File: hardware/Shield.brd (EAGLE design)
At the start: 55.9 x 47 mm, 26 parts, among them J1 AVR_SPI_PRG_6PTH, J2 TMR, J3 RELAY, Q8 TIP120, Y1 16Mhz

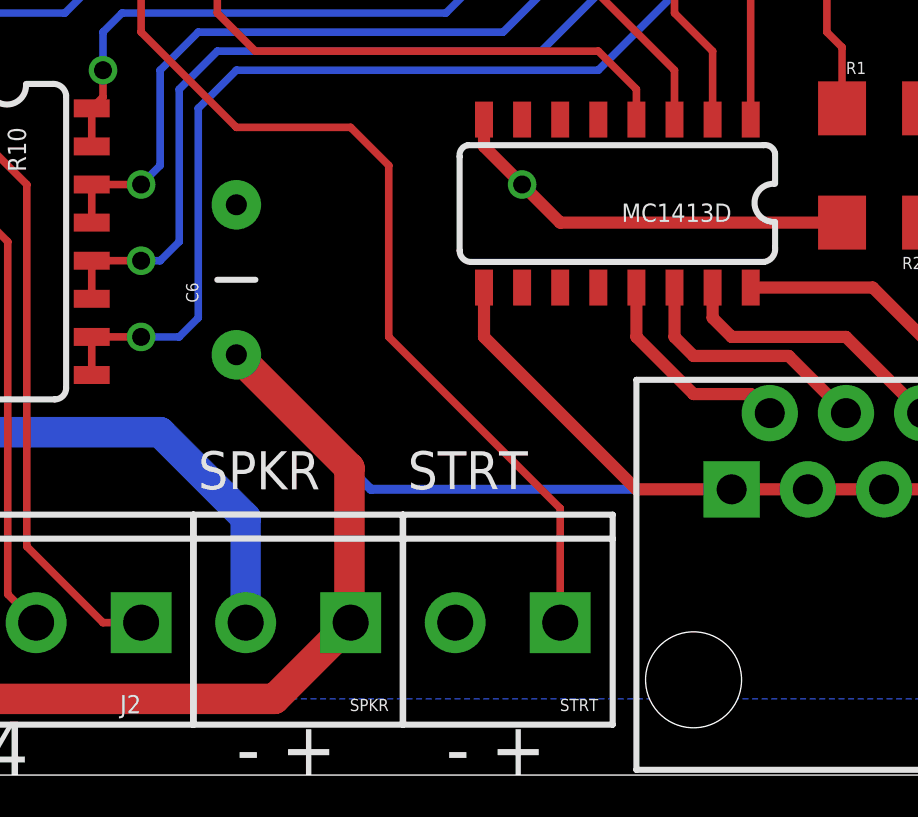
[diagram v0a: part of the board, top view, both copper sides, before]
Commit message: Moved main cap
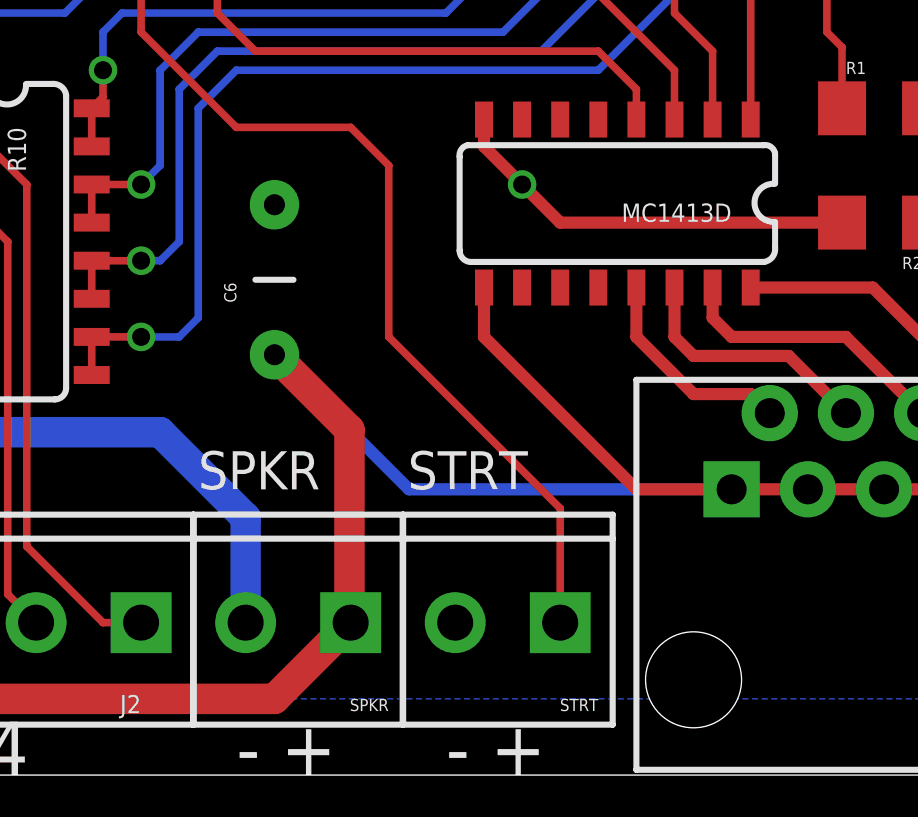
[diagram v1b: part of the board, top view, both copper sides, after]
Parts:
- moved C6 1.27 mm to (45.7, 16.5)
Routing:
- net VCC: track 170.5 -> 168.7 mm
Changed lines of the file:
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@@
 <element name="R1" library="SparkFun-Passives" package="1206" value="1K" x="66.04" y="22.225"/>
 <element name="R2" library="SparkFun-Passives" package="1206" value="2K" x="66.04" y="18.415" rot="R180"/>
-<element name="C6" library="SparkFun-Capacitors" package="CAP-PTH-5MM" value="1500uf" x="44.45" y="16.51" rot="R90"/>
+<element name="C6" library="SparkFun-Capacitors" package="CAP-PTH-5MM" value="1500uf" x="45.72" y="16.51" rot="R90"/>
 <element name="Y1" library="SparkFun-FreqCtrl" package="HC49US" value="16Mhz" x="43.815" y="41.275"/>
 <element name="C1" library="SparkFun-Capacitors" package="1206" value="22pf" x="52.07" y="41.275" rot="R90"/>
@@
 <wire x1="20.32" y1="41.91" x2="19.685" y2="42.545" width="1.016" layer="1"/>
 <contactref element="PMR2" pad="1"/>
-<wire x1="48.22" y1="5.12" x2="48.22" y2="10.24" width="1.016" layer="1"/>
-<wire x1="48.22" y1="10.24" x2="44.45" y2="14.01" width="1.016" layer="1"/>
 <wire x1="24.765" y1="2.54" x2="27.305" y2="5.08" width="1.016" layer="1"/>
-<wire x1="60.96" y1="9.525" x2="48.935" y2="9.525" width="0.3048" layer="16"/>
-<wire x1="48.935" y1="9.525" x2="44.45" y2="14.01" width="0.3048" layer="16"/>
+<wire x1="48.22" y1="5.12" x2="48.22" y2="11.51" width="1.016" layer="1"/>
+<wire x1="48.22" y1="11.51" x2="45.72" y2="14.01" width="1.016" layer="1"/>
+<wire x1="60.96" y1="9.525" x2="50.205" y2="9.525" width="0.4064" layer="16"/>
+<wire x1="50.205" y1="9.525" x2="45.72" y2="14.01" width="0.4064" layer="16"/>
 </signal>
 <signal name="D7">

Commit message: Fixed positive and negative labels
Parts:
- C3: value 0.1uf -> 10uf
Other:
- board text added: "UCI Gate v4.4-RAM"
- board text removed: "UCI Gate v4.3-RAM"
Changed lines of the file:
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@@
 <wire x1="73.66" y1="46.99" x2="17.78" y2="46.99" width="0" layer="20"/>
 <wire x1="17.78" y1="46.99" x2="17.78" y2="0" width="0" layer="20"/>
-<text x="50.165" y="43.815" size="1.778" layer="22" rot="MR0">UCI Gate v4.3-RAM</text>
+<text x="50.165" y="43.815" size="1.778" layer="22" rot="MR0">UCI Gate v4.4-RAM</text>
 <text x="51.435" y="0" size="1.778" layer="21">- +</text>
 <text x="44.45" y="0" size="1.778" layer="21">- +</text>
@@
 <text x="29.845" y="0" size="1.778" layer="21">1 2 3 4</text>
 <text x="20.955" y="36.83" size="1.27" layer="21">PWR</text>
-<text x="20.32" y="45.339" size="1.778" layer="21">- +</text>
+<text x="24.765" y="46.99" size="1.778" layer="21" rot="R180">- +</text>
 <text x="19.685" y="13.335" size="1.778" layer="21" rot="R90">+ IN -</text>
 </plain>
@@
 <element name="C1" library="SparkFun-Capacitors" package="1206" value="22pf" x="52.07" y="41.275" rot="R90"/>
 <element name="C2" library="SparkFun-Capacitors" package="1206" value="22pf" x="35.56" y="41.275" rot="R90"/>
-<element name="C3" library="SparkFun-Capacitors" package="1206" value="0.1uf" x="32.385" y="41.275" rot="R90"/>
+<element name="C3" library="SparkFun-Capacitors" package="1206" value="10uf" x="32.385" y="41.275" rot="R90"/>
 <element name="C7" library="SparkFun-Capacitors" package="CAP-PTH-SMALL" value="10uf" x="58.42" y="38.735"/>
 <element name="C8" library="SparkFun-Capacitors" package="CAP-PTH-SMALL" value="10uf" x="58.42" y="43.815"/>
@@
 <vertex x="71.12" y="2.54"/>
 <vertex x="20.32" y="2.54"/>
-<vertex x="20.32" y="45.72"/>
+<vertex x="20.32" y="43.18"/>
 <vertex x="71.12" y="45.72"/>
 </polygon>

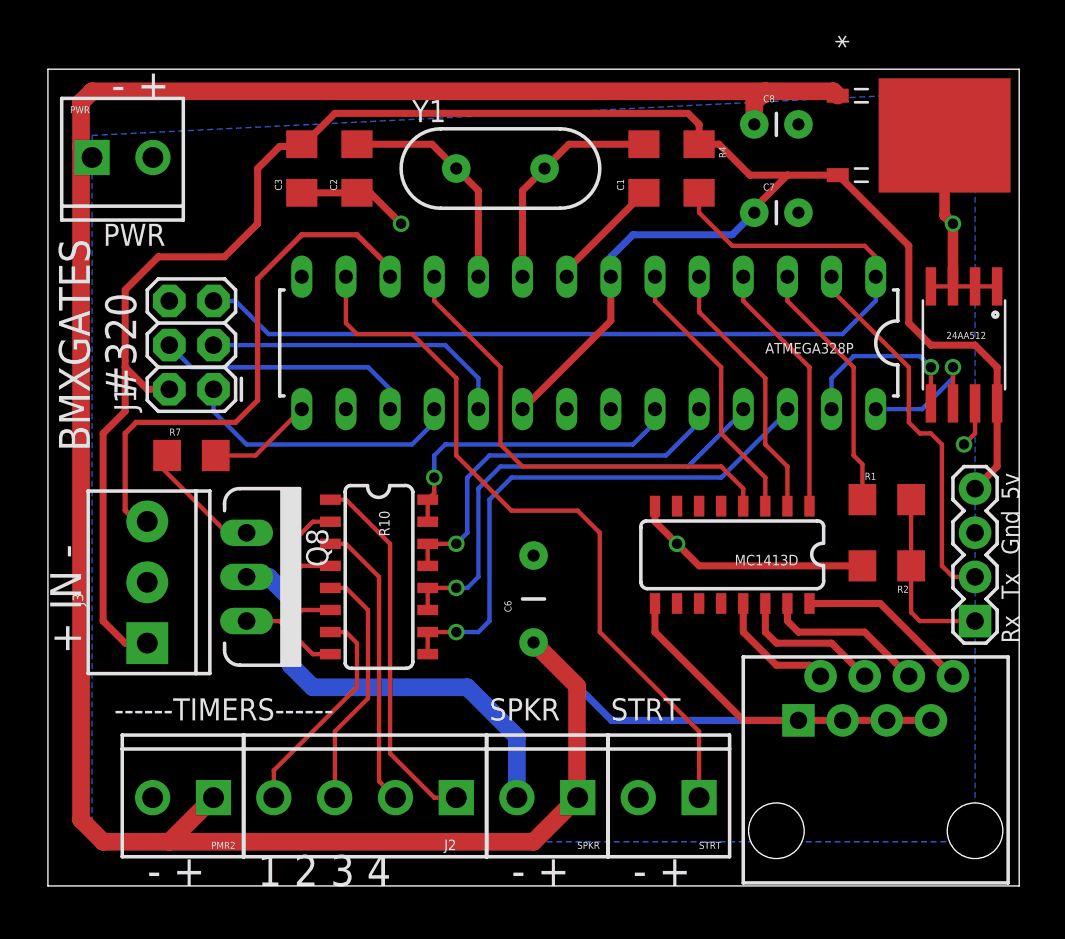
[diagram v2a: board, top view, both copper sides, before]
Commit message: Fixed gnd plan shape
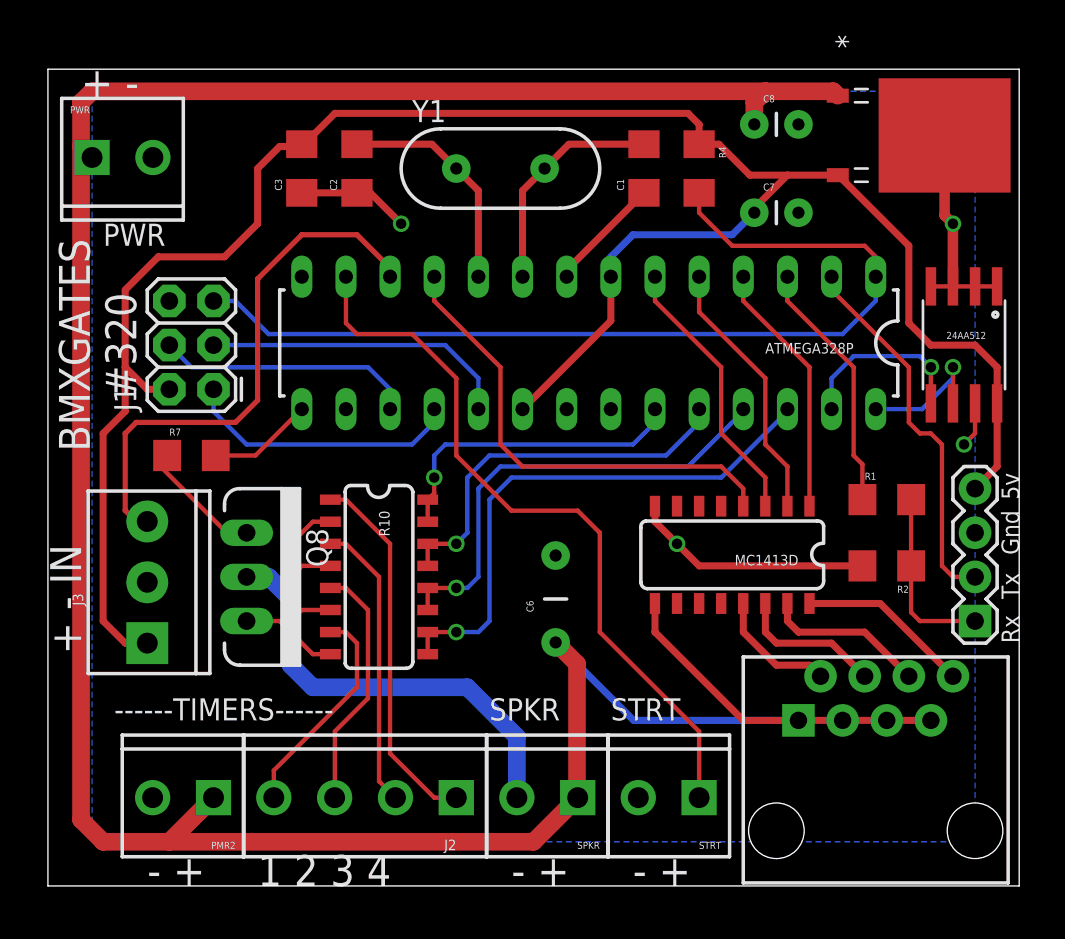
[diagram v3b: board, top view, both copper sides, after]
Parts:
- moved C6 1.27 mm to (47.0, 16.5)
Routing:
- net VCC: track 168.7 -> 166.9 mm
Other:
- board text added: "+ -"
- board text added: "+ - IN"
- board text removed: "+ IN -"
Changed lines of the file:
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@@
 <text x="29.845" y="0" size="1.778" layer="21">1 2 3 4</text>
 <text x="20.955" y="36.83" size="1.27" layer="21">PWR</text>
-<text x="24.765" y="46.99" size="1.778" layer="21" rot="R180">- +</text>
-<text x="19.685" y="13.335" size="1.778" layer="21" rot="R90">+ IN -</text>
+<text x="19.685" y="45.339" size="1.778" layer="21" distance="49">+ -</text>
+<text x="19.685" y="13.335" size="1.778" layer="21" rot="R90">+ - IN</text>
 </plain>
 <attributes>
@@
 <element name="R1" library="SparkFun-Passives" package="1206" value="1K" x="66.04" y="22.225"/>
 <element name="R2" library="SparkFun-Passives" package="1206" value="2K" x="66.04" y="18.415" rot="R180"/>
-<element name="C6" library="SparkFun-Capacitors" package="CAP-PTH-5MM" value="1500uf" x="45.72" y="16.51" rot="R90"/>
+<element name="C6" library="SparkFun-Capacitors" package="CAP-PTH-5MM" value="1500uf" x="46.99" y="16.51" rot="R90"/>
 <element name="Y1" library="SparkFun-FreqCtrl" package="HC49US" value="16Mhz" x="43.815" y="41.275"/>
 <element name="C1" library="SparkFun-Capacitors" package="1206" value="22pf" x="52.07" y="41.275" rot="R90"/>
@@
 <vertex x="71.12" y="2.54"/>
 <vertex x="20.32" y="2.54"/>
-<vertex x="20.32" y="43.18"/>
+<vertex x="20.32" y="45.72"/>
 <vertex x="71.12" y="45.72"/>
 </polygon>
@@
 <contactref element="PMR2" pad="1"/>
 <wire x1="24.765" y1="2.54" x2="27.305" y2="5.08" width="1.016" layer="1"/>
-<wire x1="48.22" y1="5.12" x2="48.22" y2="11.51" width="1.016" layer="1"/>
-<wire x1="48.22" y1="11.51" x2="45.72" y2="14.01" width="1.016" layer="1"/>
-<wire x1="60.96" y1="9.525" x2="50.205" y2="9.525" width="0.4064" layer="16"/>
-<wire x1="50.205" y1="9.525" x2="45.72" y2="14.01" width="0.4064" layer="16"/>
+<wire x1="46.99" y1="14.01" x2="51.475" y2="9.525" width="0.4064" layer="16"/>
+<wire x1="51.475" y1="9.525" x2="60.96" y2="9.525" width="0.4064" layer="16"/>
+<wire x1="48.22" y1="5.12" x2="48.22" y2="12.78" width="1.016" layer="1"/>
+<wire x1="48.22" y1="12.78" x2="46.99" y2="14.01" width="1.016" layer="1"/>
 </signal>
 <signal name="D7">
